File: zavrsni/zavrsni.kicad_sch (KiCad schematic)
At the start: 0 parts

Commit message: schematics
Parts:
- added C1: 15n, Capacitor_THT:C_Disc_D5.0mm_W2.5mm_P2.50mm, symbol Device:C_Small
- added C10, C11, C14, C15, C17, C18, C4, C8: 100n, Capacitor_THT:C_Disc_D5.0mm_W2.5mm_P5.00mm, symbol Device:C_Small
- added C12, C13, C16, C19, C2, C3, C7: 10u, Capacitor_THT:CP_Radial_D5.0mm_P2.50mm, symbol Device:C_Polarized_Small
- added C20: 100u, Capacitor_THT:CP_Radial_D5.0mm_P2.50mm, symbol Device:C_Polarized_Small
- added C5, C6, C9: 680u, Capacitor_THT:CP_Radial_D8.0mm_P2.50mm, symbol Device:C_Polarized_Small
- added D1, D2: 1N4148, Diode_THT:D_DO-35_SOD27_P7.62mm_Horizontal, symbol Diode:1N4148
- added H1, H2, H3, H4: MountingHole_Pad, MountingHole:MountingHole_4.3mm_M4_ISO7380_Pad, symbol Mechanical:MountingHole_Pad
- added Jin1: Conn_01x01_Pin, Connector_Wire:SolderWirePad_1x01_SMD_3x6mm, symbol Connector:Conn_01x01_Pin
- added Q1: BC337, Package_TO_SOT_THT:TO-92_Inline, symbol Simulation_SPICE:NPN
- added Q2: PNP, Package_TO_SOT_THT:TO-92_Inline, symbol Simulation_SPICE:PNP
- added R1, R2: 300, Resistor_THT:R_Axial_DIN0207_L6.3mm_D2.5mm_P10.16mm_Horizontal, symbol Device:R
- added R10, R11, R3, R4, R8: 10k, Resistor_THT:R_Axial_DIN0207_L6.3mm_D2.5mm_P10.16mm_Horizontal, symbol Device:R
- added R12, R13, R5, R9: 1k, Resistor_THT:R_Axial_DIN0207_L6.3mm_D2.5mm_P10.16mm_Horizontal, symbol Device:R
- added R6: 330, Resistor_THT:R_Axial_DIN0207_L6.3mm_D2.5mm_P10.16mm_Horizontal, symbol Device:R
- added R7: 3k3, Resistor_THT:R_Axial_DIN0207_L6.3mm_D2.5mm_P10.16mm_Horizontal, symbol Device:R
- added SW1: RotaryEncoder_Switch, Rotary_Encoder:RotaryEncoder_Alps_EC11E-Switch_Vertical_H20mm_CircularMountingHoles, symbol Device:RotaryEncoder_Switch
- added SW2, SW3, SW4, SW5, SW6, SW7, SW8, SW9: SW_Push, Button_Switch_THT:SW_PUSH_6mm_H13mm, symbol Switch:SW_Push
- added U1: PCM3060, Package_DIP:DIP-28_W15.24mm_Socket, symbol Audio:PCM3060
- added U2: WeAct STM32F411CEU6 v3.0, Package_DIP:DIP-40_W15.24mm_Socket, symbol ljepe:WeActSTM32F411CEU6
- added U3: NE5532, Package_DIP:DIP-8_W7.62mm_Socket, symbol Amplifier_Operational:NE5532
- added U4: TL074, symbol Amplifier_Operational:TL074
- added U5: LM358, symbol Amplifier_Operational:LM358
- added U6: LM317_TO-220, Package_TO_SOT_THT:TO-220-3_Vertical, symbol Regulator_Linear:LM317_TO-220
- added U7: UC1609C LCD Board, ljepi:PinSocket1x9_66mm_x_26mm, symbol ljepe:UC1609C_Board
- added U8: 74HC595, Package_DIP:DIP-16_W7.62mm_Socket, symbol 74xx:74HC595
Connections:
- new net: R1.1, U3.1, U3.2 (-)
- new net: C2.2, R2.2, U3.5 (+)
- new net: R5.2, R6.1, U3.6 (-)
- new net: C7.1, R5.1, U3.7
- new net: R7.2, R8.1, U6.1 (ADJ)
- new net: R10.1, R11.2, U4.3 (+)
- new net: C1.1, C2.1, R1.2
- new net: C16.1, C17.2, U1.21 (V_{COM})
- new net: C7.2, R12.2
- new net: Q1.2 (B), Q2.2 (B), U5.1, U5.2 (-)
- new net: U2.36 (B2), U7.4 (VDD)
- new net: U2.31 (A5), U7.5 (SCK)
- new net: U2.33 (A7), U7.6 (SDA)
- new net: U2.37 (B10), U7.7 (RST)
- new net: U2.35 (B1), U7.8 (CD)
- new net: U2.34 (B0), U7.9 (CS)
- new net: D1.2 (A), D2.1 (K), R9.1, U4.12 (+), U4.6 (-), U4.9 (-)
- new net: U1.25 (V_{IN}L), U1.26 (V_{IN}R), U4.13 (-), U4.14
- new net: D1.1 (K), U4.7
- new net: R12.1, R13.2, U4.2 (-)
- new net: R3.1, R4.2, U5.3 (+)
- new net: R13.1, R9.2, U4.1
- new net: U8.13 (~{OE}), U8.16 (VCC)
- new net: D2.2 (A), U4.8
- new net +0V: C10.2, C11.2, C3.2, C4.2, C6.2, C8.2, C9.2, Q2.3 (E), R4.1, U3.4 (V-), U4.11 (V-), U5.4 (V-)
- new net +12V: C10.1, C11.1, C3.1, C4.1, C5.1, C8.1, C9.1, Q1.1 (C), R3.2, U3.8 (V+), U4.4 (V+), U5.8 (V+), U6.3 (VI)
- new net +3V3: C13.1, C14.2, C18.1, C19.1, C20.1, U1.7 (V_{DD}), U2.20 (3V3), U7.2 (A)
- new net +5V: C12.1, C15.2, R10.2, R7.1, U1.24 (V_{CC}), U4.10 (+), U6.2 (VO)
- new net GNDREF: C1.2, C12.2, C13.2, C14.1, C15.1, C16.2, C17.1, C18.2, C19.2, C20.2, C5.2, C6.1, H1.1, H2.1, H3.1, H4.1, Q1.3 (E), Q2.1 (C), R11.1, R2.1, R6.2, R8.2, SW1.C, SW1.S2, SW2.2, SW3.2, SW4.2, SW5.2, SW6.2, SW7.2, SW8.2, SW9.2, U1.16 (SGND), U1.22 (AGND2), U1.23 (AGND1), U1.8 (DGND), U2.19 (GND), U4.5 (+), U7.1 (K), U7.3 (GND)
- new net IN: Jin1.1 (Pin_1), U3.3 (+)
- no-connect marks 0 -> 1
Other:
- note added: "Ograničavanje napona zvučnog signala između 0V i +5V"
- note added: "Pojasno propusni filtar ~40Hz <-> ~20kHz"
- note added: "Pojačavanje & pomicanje zvučnog signala za +2.5V"
- note added: "Razdvajač jednopolarnog napajanja (+12V, 0V --> +6V, 0V, -6V)"
- note added: "Regulator napona +6V --> +~5V"
- note added: "Ulazni razdvojnik (buffer)"

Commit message: PCM3060 basic interface
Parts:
- removed U8: 74HC595, Package_DIP:DIP-16_W7.62mm_Socket, symbol 74xx:74HC595
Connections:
- net GNDREF: now also U1.15 (~{RST}), U1.27 (~{MS}/AD/IFMD), U1.28 (MODE)
- net PCM_ADC_LR: now reaches U2.1 (B12)
- net PCM_ADC_LR: now also U1.4 (LRCK1)
- net PCM_SCKI: now reaches U2.10 (A15)
- net PCM_SCKI: now also U1.6 (SCKI1), U1.9 (SCKI2)
- net PCM_DAC_BCK: now reaches U2.11 (B3)
- net PCM_DAC_BCK: now also U1.10 (BCK2)
- net PCM_DAC_DIN: now reaches U2.13 (B5)
- net PCM_DAC_DIN: now also U1.12 (DIN)
- net PCM_SCL: now reaches U2.14 (B6)
- net PCM_SCL: now also U1.1 (MC/SCL/FMT)
- net PCM_SDA: now reaches U2.15 (B7)
- net PCM_SDA: now also U1.2 (MD/SDA/DEMP)
- net PCM_ADC_BCK: now reaches U2.2 (B13)
- net PCM_ADC_BCK: now also U1.5 (BCK1)
- net PCM_DAC_LR: now reaches U2.30 (A4)
- net PCM_DAC_LR: now also U1.11 (LRCK2)
- net PCM_ADC_DOUT: now reaches U2.4 (B15)
- net PCM_ADC_DOUT: now also U1.3 (DOUT)
- no-connect marks 1 -> 5
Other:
- moved on the sheet: C1, C12, C13, C14, C15, C16, C17, C18, C19, C2, C20, C7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

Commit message: switch to SPI interface instead of I2C for PCM3060
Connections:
- net +3V3: now also U1.28 (MODE)
- net GNDREF: no longer U1.15 (~{RST}), U1.27 (~{MS}/AD/IFMD), U1.28 (MODE)
- new net PCM_CS: U1.27 (~{MS}/AD/IFMD)
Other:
- note added: "SPI"
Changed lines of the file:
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@@
 		)
 	)
+	(text "SPI"
+		(exclude_from_sim no)
+		(at 347.218 251.968 0)
+		(effects
+			(font
+				(size 1.27 1.27)
+			)
+		)
+	)
 	(text "Ograničavanje napona zvučnog signala između 0V i +5V"
 		(exclude_from_sim no)
@@
 	)
 	(junction
-		(at 349.25 254)
-		(diameter 0)
-		(color 0 0 0 0)
-	)
-	(junction
 		(at 44.45 133.35)
 		(diameter 0)
@@
 	)
 	(junction
-		(at 347.98 226.06)
-		(diameter 0)
-		(color 0 0 0 0)
-	)
-	(junction
 		(at 179.07 157.48)
 		(diameter 0)
@@
 	(wire
 		(pts
-			(xy 349.25 254) (xy 350.52 254)
-		)
-		(stroke
-			(width 0)
-			(type default)
-		)
-	)
-	(wire
-		(pts
 			(xy 425.45 194.31) (xy 425.45 193.04)
 		)
@@
 	(wire
 		(pts
-			(xy 336.55 196.85) (xy 336.55 243.84)
+			(xy 335.28 248.92) (xy 350.52 248.92)
 		)
 		(stroke
@@
 	(wire
 		(pts
-			(xy 217.17 290.83) (xy 160.02 290.83)
+			(xy 336.55 196.85) (xy 336.55 243.84)
 		)
 		(stroke
@@
 	(wire
 		(pts
-			(xy 179.07 143.51) (xy 179.07 139.7)
+			(xy 217.17 290.83) (xy 160.02 290.83)
 		)
 		(stroke
@@
 	(wire
 		(pts
-			(xy 30.48 207.01) (xy 33.02 207.01)
+			(xy 179.07 143.51) (xy 179.07 139.7)
 		)
 		(stroke
@@
 	(wire
 		(pts
-			(xy 44.45 133.35) (xy 44.45 143.51)
+			(xy 30.48 207.01) (xy 33.02 207.01)
 		)
 		(stroke
@@
 	(wire
 		(pts
-			(xy 300.99 266.7) (xy 300.99 259.08)
+			(xy 44.45 133.35) (xy 44.45 143.51)
 		)
 		(stroke
@@
 	(wire
 		(pts
-			(xy 349.25 255.27) (xy 349.25 254)
+			(xy 300.99 266.7) (xy 300.99 259.08)
 		)
 		(stroke
@@
 	(wire
 		(pts
-			(xy 344.17 251.46) (xy 350.52 251.46)
-		)
-		(stroke
-			(width 0)
-			(type default)
-		)
-	)
-	(wire
-		(pts
 			(xy 523.24 309.88) (xy 524.51 309.88)
 		)
@@
 	(wire
 		(pts
-			(xy 350.52 248.92) (xy 349.25 248.92)
-		)
-		(stroke
-			(width 0)
-			(type default)
-		)
-	)
-	(wire
-		(pts
 			(xy 107.95 281.94) (xy 107.95 290.83)
 		)
@@
 	(wire
 		(pts
-			(xy 344.17 226.06) (xy 344.17 251.46)
-		)
-		(stroke
-			(width 0)
-			(type default)
-		)
-	)
-	(wire
-		(pts
 			(xy 179.07 153.67) (xy 179.07 157.48)
 		)
@@
 	(wire
 		(pts
-			(xy 349.25 248.92) (xy 349.25 254)
-		)
-		(stroke
-			(width 0)
-			(type default)
-		)
-	)
-	(wire
-		(pts
 			(xy 350.52 269.24) (xy 349.25 269.24)
 		)
@@
 	(wire
 		(pts
-			(xy 347.98 226.06) (xy 344.17 226.06)
-		)
-		(stroke
-			(width 0)
-			(type default)
-		)
-	)
-	(wire
-		(pts
 			(xy 160.02 290.83) (xy 135.89 290.83)
 		)
@@
 		)
 	)
+	(label "PCM_CS"
+		(at 342.9 248.92 0)
+		(effects
+			(font
+				(size 1.27 1.27)
+			)
+			(justify left bottom)
+		)
+	)
 	(label "PCM_ADC_LR"
 		(at 331.47 163.83 0)
@@
 	)
 	(symbol
+		(lib_id "power:+3V3")
+		(at 350.52 254 90)
+		(unit 1)
+		(exclude_from_sim no)
+		(in_bom yes)
+		(on_board yes)
+		(dnp no)
+		(fields_autoplaced yes)
+		(property "Reference" "#PWR027"
+			(at 354.33 254 0)
+			(effects
+				(font
+					(size 1.27 1.27)
+				)
+				(hide yes)
+			)
+		)
+		(property "Value" "+3V3"
+			(at 346.71 253.9999 90)
+			(effects
+				(font
+					(size 1.27 1.27)
+				)
+				(justify left)
+			)
+		)
+		(property "Footprint" ""
+			(at 350.52 254 0)
+			(effects
+				(font
+					(size 1.27 1.27)
+				)
+				(hide yes)
+			)
+		)
+		(property "Datasheet" ""
+			(at 350.52 254 0)
+			(effects
+				(font
+					(size 1.27 1.27)
+				)
+				(hide yes)
+			)
+		)
+		(property "Description" "Power symbol creates a global label with name \"+3V3\""
+			(at 350.52 254 0)
+			(effects
+				(font
+					(size 1.27 1.27)
+				)
+				(hide yes)
+			)
+		)
+		(pin "1"
+		)
+		(instances
+			(project "zavrsni"
+				(path "/22cdc1b5-9057-4680-8669-7a02483bacee"
+					(reference "#PWR027")
+					(unit 1)
+				)
+			)
+		)
+	)
+	(symbol
 		(lib_id "Device:C_Small")
 		(at 354.33 231.14 90)
@@
 					(unit 1)
 				)
-			)
-		)
-	)
-	(symbol
-		(lib_id "power:GNDREF")
-		(at 349.25 255.27 0)
-		(unit 1)
-		(exclude_from_sim no)
-		(in_bom yes)
-		(on_board yes)
-		(dnp no)
-		(fields_autoplaced yes)
-		(property "Reference" "#PWR026"
-			(at 349.25 261.62 0)
-			(effects
-				(font
-					(size 1.27 1.27)
-				)
-				(hide yes)
-			)
-		)
-		(property "Value" "GNDREF"
-			(at 349.25 260.35 0)
-			(effects
-				(font
-					(size 1.27 1.27)
-				)
-				(hide yes)
-			)
-		)
-		(property "Footprint" ""
-			(at 349.25 255.27 0)
-			(effects
-				(font
-					(size 1.27 1.27)
-				)
-				(hide yes)
-			)
-		)
-		(property "Datasheet" ""
-			(at 349.25 255.27 0)
-			(effects
-				(font
-					(size 1.27 1.27)
-				)
-				(hide yes)
-			)
-		)
-		(property "Description" "Power symbol creates a global label with name \"GNDREF\" , reference supply ground"
-			(at 349.25 255.27 0)
-			(effects
-				(font
-					(size 1.27 1.27)
-				)
-				(hide yes)
-			)
-		)
-		(pin "1"
-		)
-		(instances
-			(project "zavrsni"
-				(path "/22cdc1b5-9057-4680-8669-7a02483bacee"
-					(reference "#PWR026")
-					(unit 1)
-				)

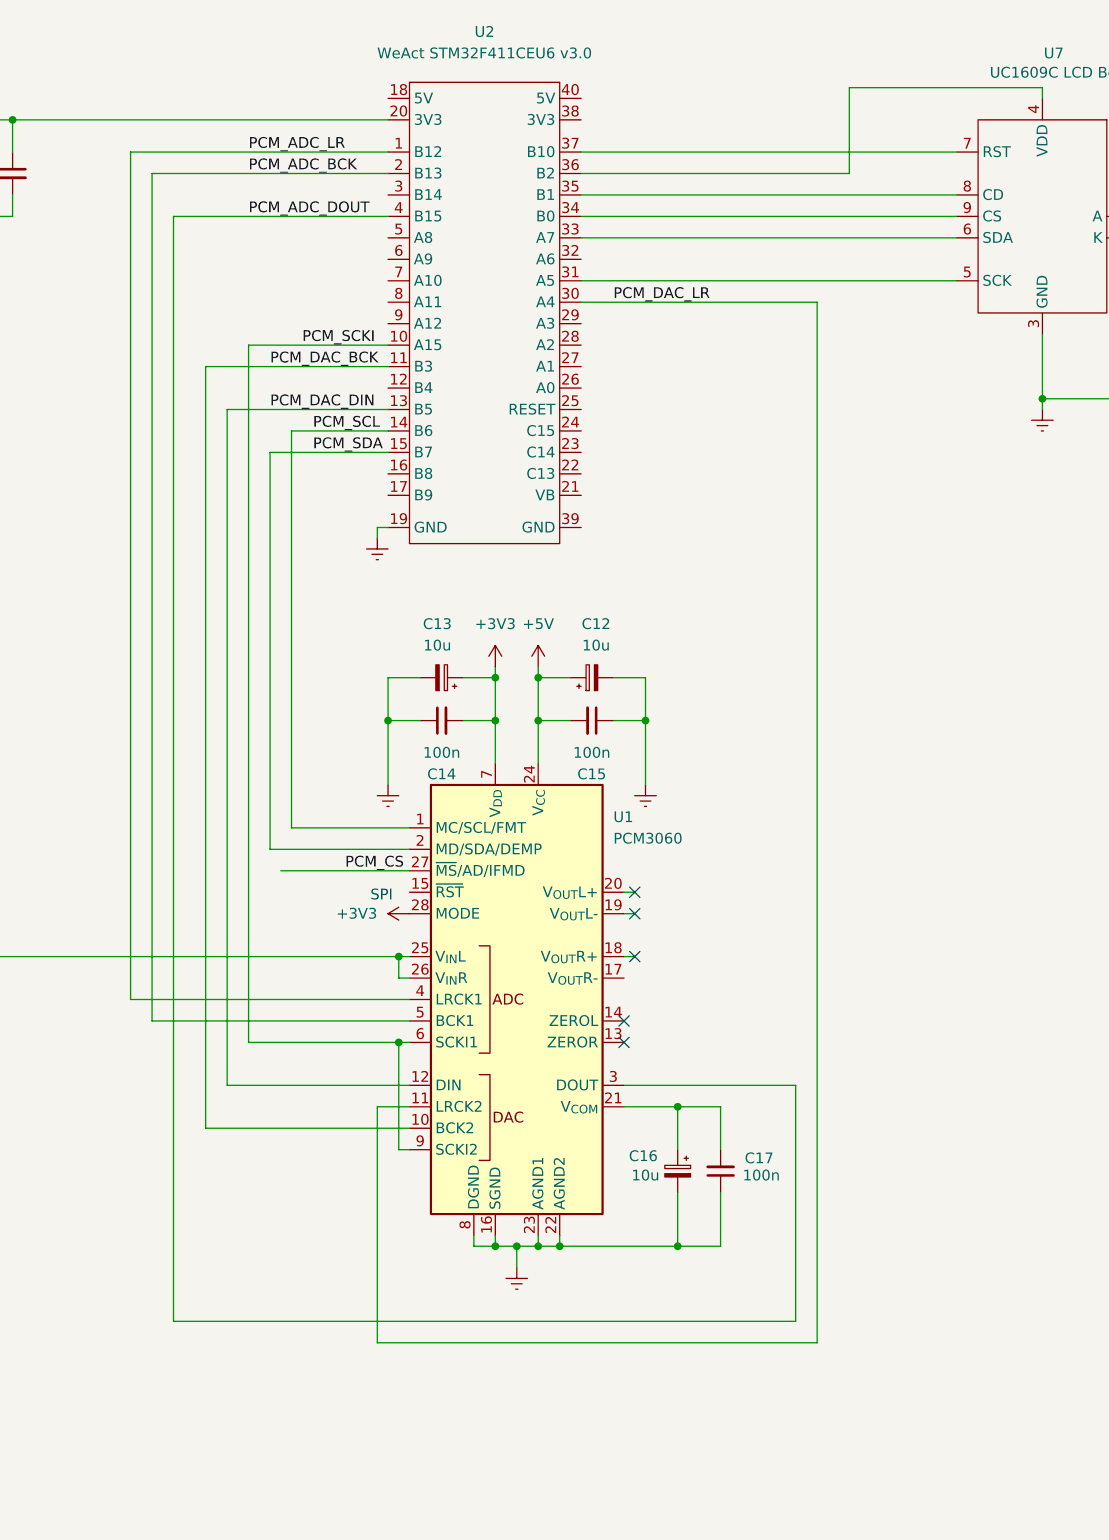
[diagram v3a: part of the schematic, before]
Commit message: back to I2C for the read functionality, still cannot get it working
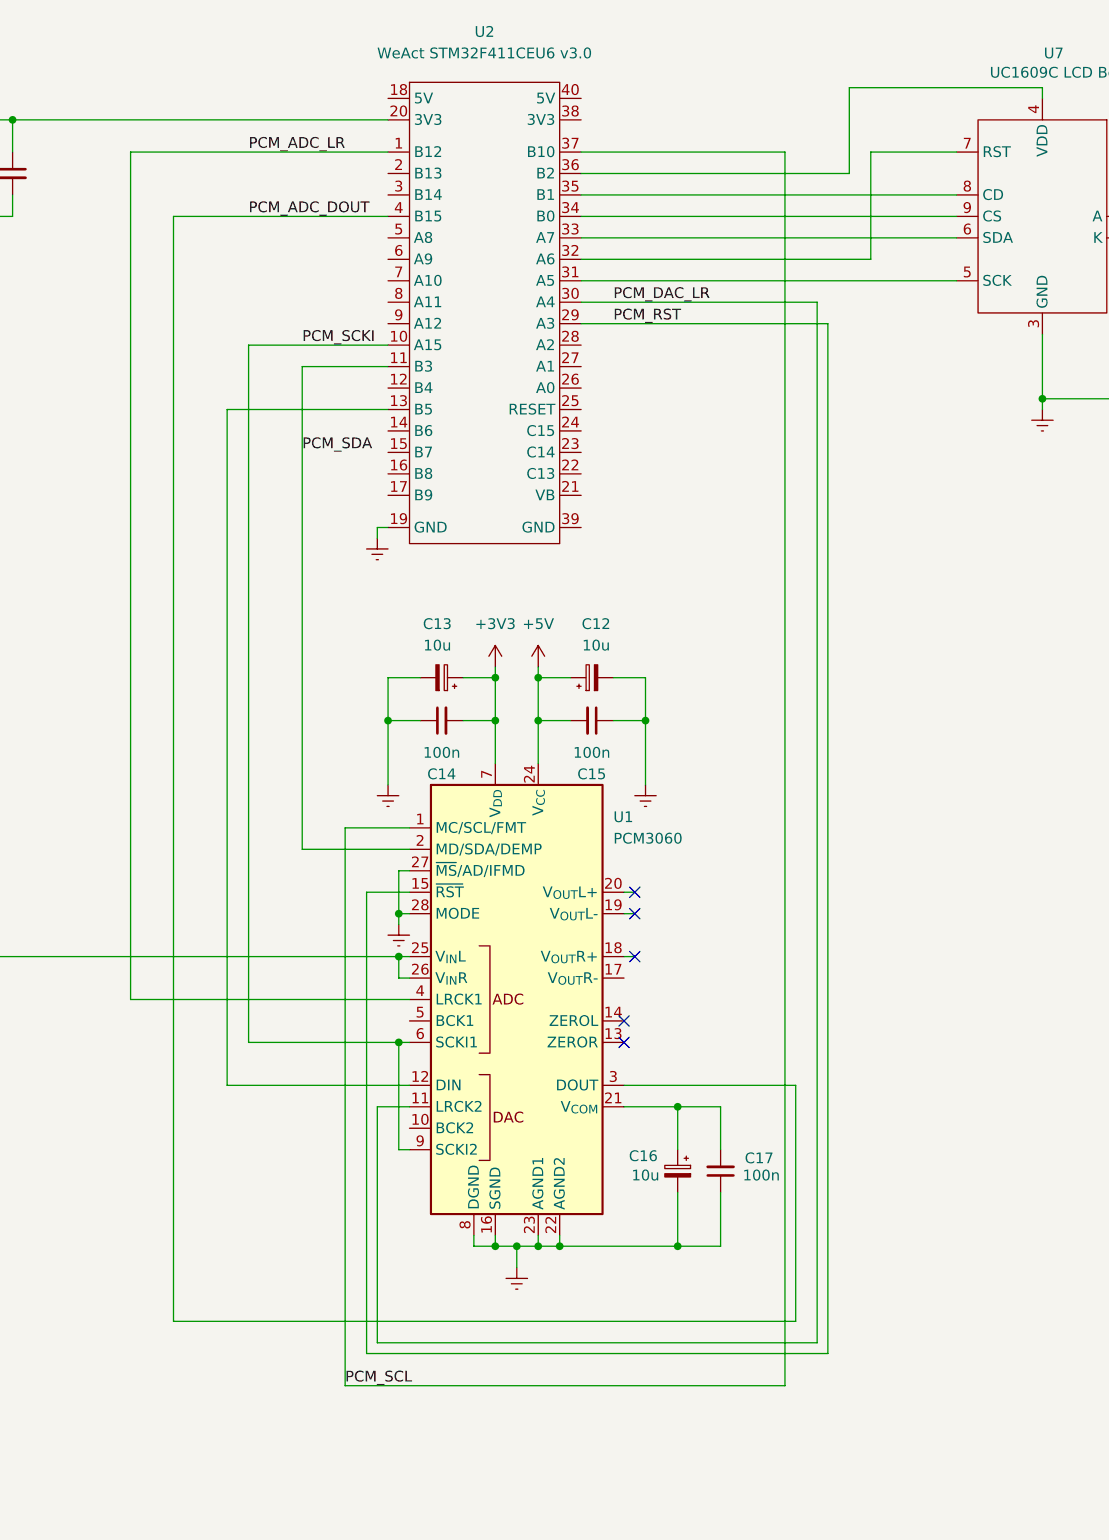
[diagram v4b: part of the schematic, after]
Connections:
- net PCM_CS is gone; now on net GNDREF: U1.27 (~{MS}/AD/IFMD)
- net +3V3: no longer U1.28 (MODE)
- net GNDREF: now also U1.28 (MODE)
- net PCM_SCL: now also U2.37 (B10); no longer U2.14 (B6)
- net PCM_SDA: now also U2.11 (B3); no longer U2.15 (B7)
- net at U7.7 (RST): now also U2.32 (A6); no longer U2.37 (B10)
- net PCM_RST: now reaches U2.29 (A3)
- net PCM_RST: now also U1.15 (~{RST})
- net PCM_ADC_BCK: no longer names the net of U2.2 (B13)
- net PCM_ADC_BCK: no longer U1.5 (BCK1)
- net PCM_DAC_BCK: no longer names the net of U1.10 (BCK2)
- net PCM_DAC_BCK: no longer U2.11 (B3)
- net PCM_DAC_DIN: no longer names the net of U1.12 (DIN), U2.13 (B5)
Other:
- note removed: "SPI"
